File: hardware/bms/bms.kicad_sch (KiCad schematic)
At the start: 41 parts, among them J1 Screw_Terminal_01x01, J10 Conn_01x10, J11 USB_C_Receptacle_USB2.0, J12 Conn_01x03, J13 Conn_01x07, J2 Screw_Terminal_01x01, J3 Screw_Terminal_01x01, J4 Screw_Terminal_01x01, J5 Screw_Terminal_01x01, J6 Conn_01x02, J7 Conn_01x10, J8 Conn_01x02, U8 USBLC6-2SC6

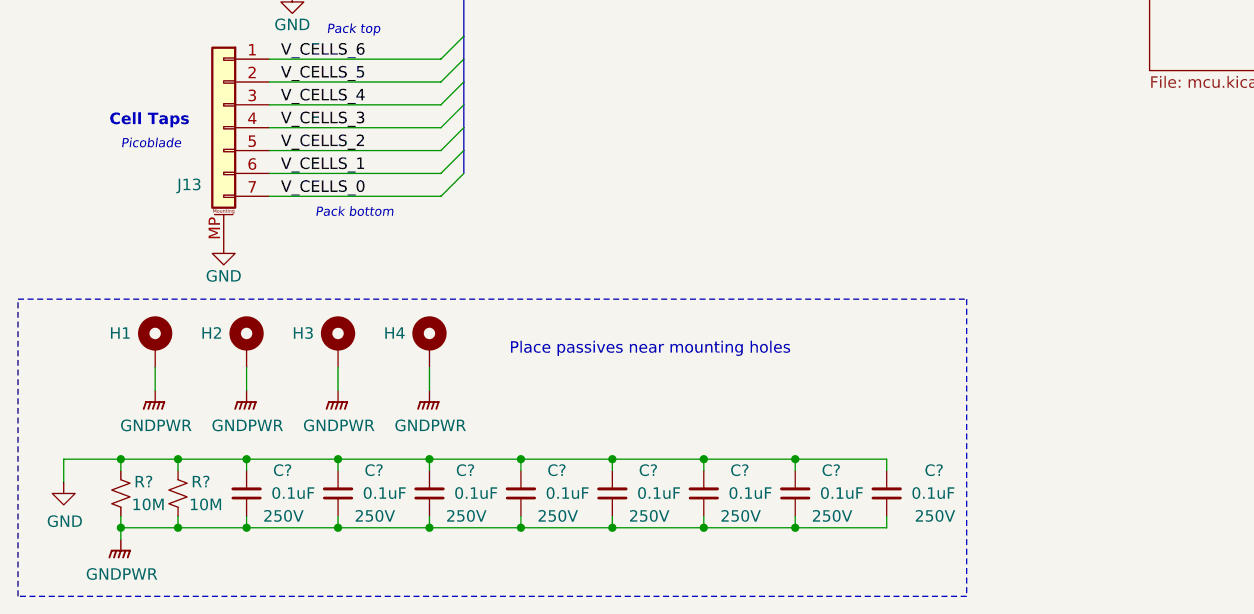
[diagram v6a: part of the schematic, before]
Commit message: Simplified chassis connection, only at one mounting hole and left other holes NC (no chassis plane on PCB
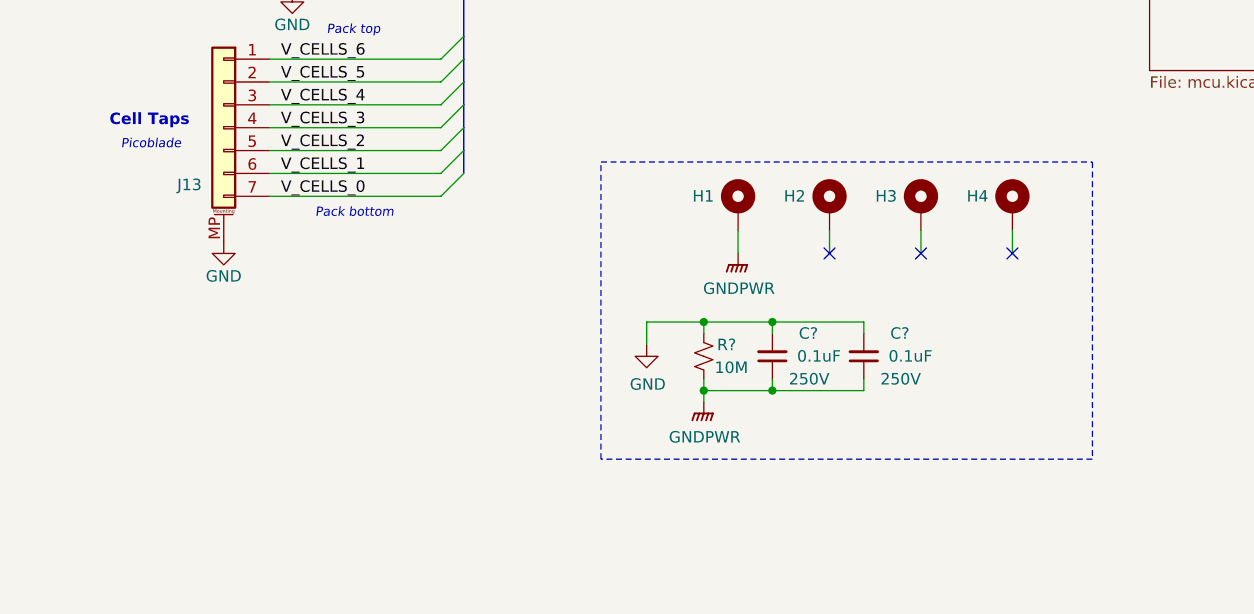
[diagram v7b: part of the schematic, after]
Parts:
- removed C? (x6): 0.1uF, Capacitor_SMD:C_0805_2012Metric, symbol Device:C_Small
- removed R?: 10M, Resistor_SMD:R_0603_1608Metric, symbol Device:R_Small_US
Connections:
- net GNDPWR: no longer H2.1, H3.1, H4.1
- no-connect marks 4 -> 7
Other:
- note removed: "Place passives near mounting holes"
- moved on the sheet: C?, H1, H2, H3, H4, R?

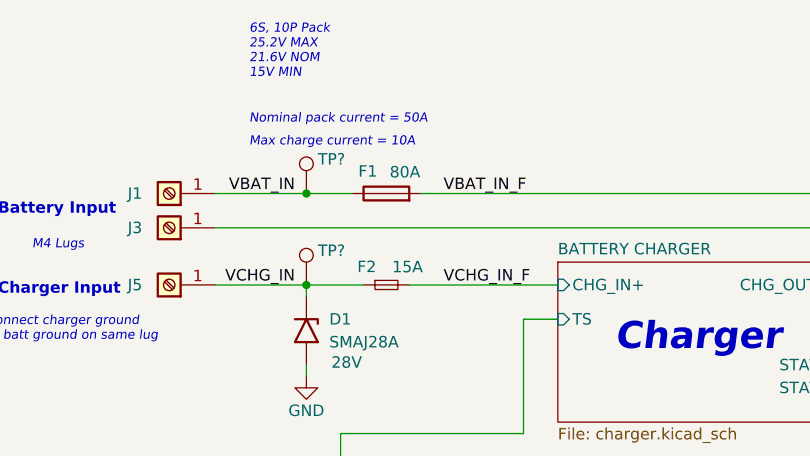
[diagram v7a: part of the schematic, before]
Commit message: Changed large input fuse, slightly smaller and cheaper, 60A rated. Layout more defined, charger layout much better now
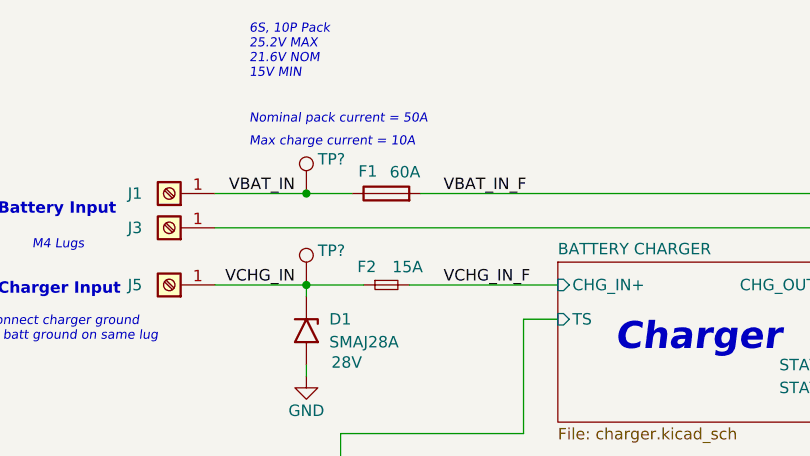
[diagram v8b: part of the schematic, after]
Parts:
- F1: value 80A -> 60A; footprint bms:FUSE_0ACH-9800-TE_BEL -> bms:SF-3812F6000T-2; MFG Bel Fuse Inc. -> Bourns Inc.; MFG PN 0ACH-9800-TE -> SF-3812F6000T-2
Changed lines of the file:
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@@
       (effects (font (size 1.27 1.27)))
     )
-    (property "Value" "80A" (at 65.5679 34.4546 90)
+    (property "Value" "60A" (at 65.5679 34.4546 90)
       (effects (font (size 1.27 1.27)))
     )
-    (property "Footprint" "bms:FUSE_0ACH-9800-TE_BEL" (at 63.5 38.608 90)
+    (property "Footprint" "bms:SF-3812F6000T-2" (at 63.5 38.608 90)
       (effects (font (size 1.27 1.27)) hide)
     )
@@
       (effects (font (size 1.27 1.27)) hide)
     )
-    (property "MFG" "Bel Fuse Inc." (at 63.5 36.83 90)
+    (property "MFG" "Bourns Inc." (at 63.5 36.83 90)
       (effects (font (size 1.27 1.27)) hide)
     )
-    (property "MFG PN" "0ACH-9800-TE" (at 63.5 36.83 90)
+    (property "MFG PN" "SF-3812F6000T-2" (at 63.5 36.83 90)
       (effects (font (size 1.27 1.27)) hide)
     )
